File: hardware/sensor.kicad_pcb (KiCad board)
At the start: 2 copper layers, 10 parts, among them U1 ESP32-WROOM, U2 AP2112K-3.3TRG1, U3 BME280

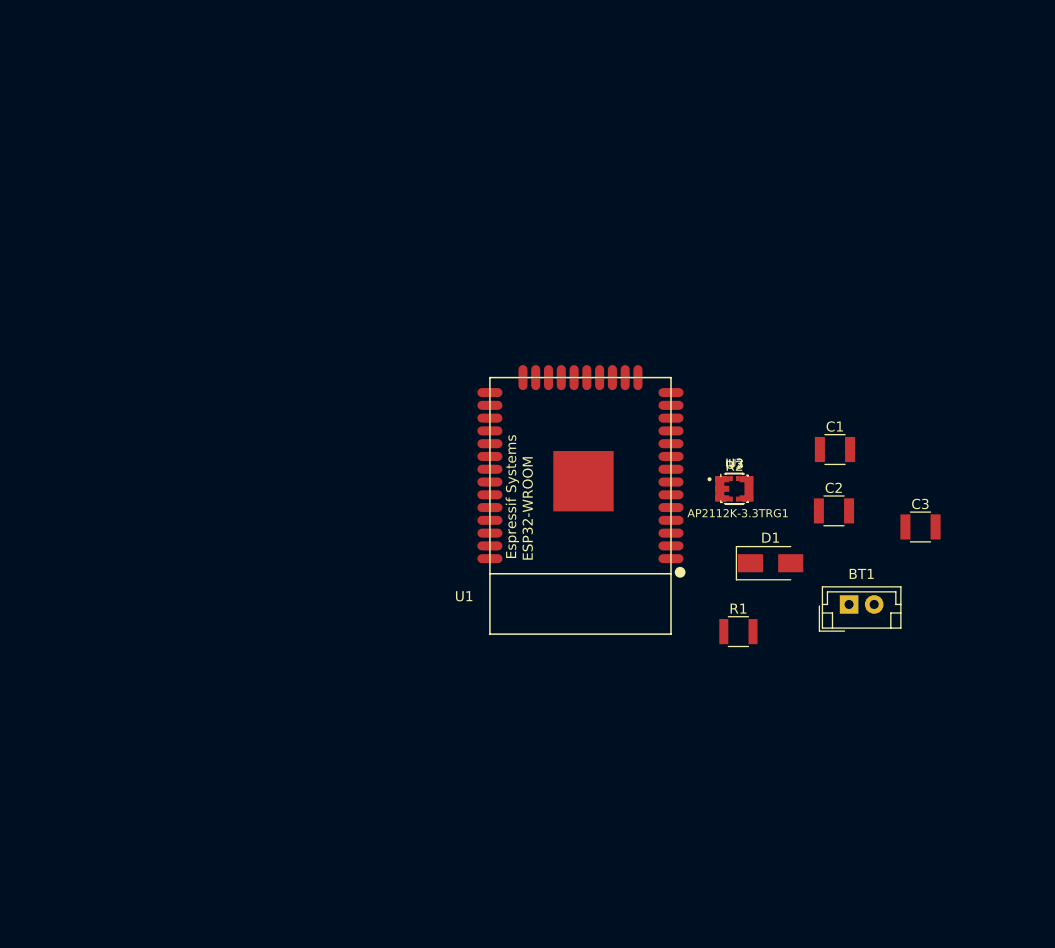
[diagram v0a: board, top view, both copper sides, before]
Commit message: Continue schematic work
Cleanup power
Add I2C connectors
Connect BME280 w/ I2C
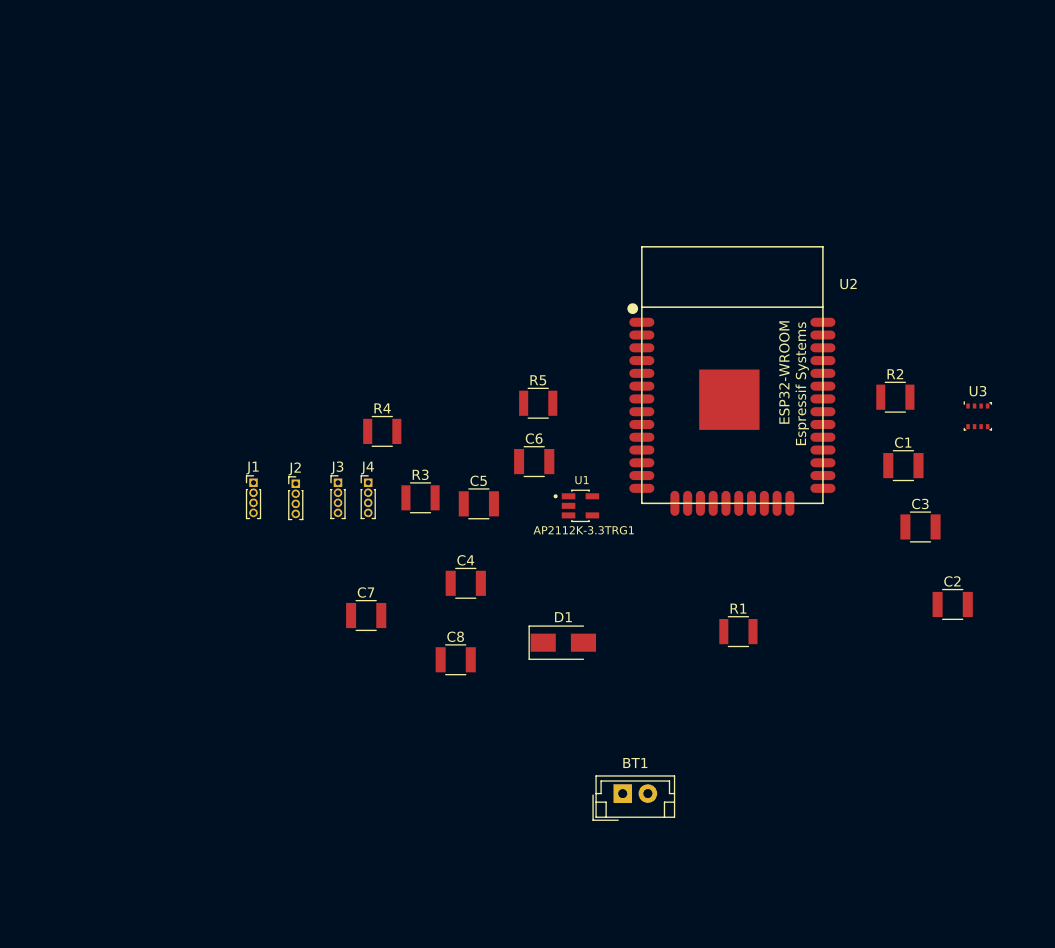
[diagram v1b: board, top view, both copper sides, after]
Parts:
- added C4: 1uF, Capacitors_SMD:C_1210, F.Cu at (121.8, 114.4)
- added C5: 10uF, Capacitors_SMD:C_1210, F.Cu at (123.1, 106.5)
- added C6: 0.1uF, Capacitors_SMD:C_1210, F.Cu at (128.6, 102.3)
- added C7: 100nF, Capacitors_SMD:C_1210, F.Cu at (111.9, 117.6)
- added C8: 100nF, Capacitors_SMD:C_1210, F.Cu at (120.8, 122.0)
- added J1: Conn_01x04, Pin_Headers:Pin_Header_Straight_1x04_Pitch1.00mm, F.Cu at (100.7, 104.4)
- added J2: Conn_01x04, Pin_Headers:Pin_Header_Straight_1x04_Pitch1.00mm, F.Cu at (104.9, 104.5)
- added J3: Conn_01x04, Pin_Headers:Pin_Header_Straight_1x04_Pitch1.00mm, F.Cu at (109.1, 104.4)
- added J4: Conn_01x04, Pin_Headers:Pin_Header_Straight_1x04_Pitch1.00mm, F.Cu at (112.1, 104.4)
- added R3: 10k, Resistors_SMD:R_1210, F.Cu at (117.3, 105.9)
- added R4: 4.7k, Resistors_SMD:R_1210, F.Cu at (113.5, 99.3)
- added R5: 4.7k, Resistors_SMD:R_1210, F.Cu at (129.0, 96.5)
- C2: value 10uF -> 0.1uF
- C3: value 1uF -> 10uF
- U1: value ESP32-WROOM -> AP2112K-3.3TRG1; footprint ESP32-footprints-Lib:ESP32-WROOM -> AP2112K-3.3TRG1:SOT95P285X140-5N
- U2: value AP2112K-3.3TRG1 -> ESP32-WROOM; footprint AP2112K-3.3TRG1:SOT95P285X140-5N -> ESP32-footprints-Lib:ESP32-WROOM
- moved BT1 29.3 mm to (137.4, 135.3)
- moved U3 25.2 mm to (172.7, 97.8)
- moved D1 22.1 mm to (131.5, 120.3)
- moved R2 18.4 mm to (164.5, 95.9)
- moved C2 15.0 mm to (170.2, 116.5)
- moved U2 11.3 mm to (148.3, 93.7), turned to 180 degrees
- moved C1 6.99 mm to (165.3, 102.7)
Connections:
- C2 pad 1: VCC -> Net-(C2-Pad1)
- U1 pad 1: GND -> Net-(C1-Pad1)
- U1 pad 2: VCC -> GND
- U1 pad 3: VCC -> Net-(C1-Pad1)
- U1 pad 5: (no net) -> VCC
- U2 pad 1: Net-(C1-Pad1) -> GND
- U2 pad 2: GND -> VCC
- U2 pad 3: Net-(C1-Pad1) -> Net-(C2-Pad1)
- U2 pad 5: VCC -> (no net)
- U3 pad 2: (no net) -> VCC
- U3 pad 3: (no net) -> iic1_sda
- U3 pad 4: (no net) -> iic1_clk
- U3 pad 5: (no net) -> GND

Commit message: Continue HW design
* Setup SPI expansion connectors
* Re-annotate caps for power regulator and WROOM power
* Add globals for JTAG pins
* Rough grouping of parts on PCB
- Note - still need to make battery setup choices and footprint choices for passives
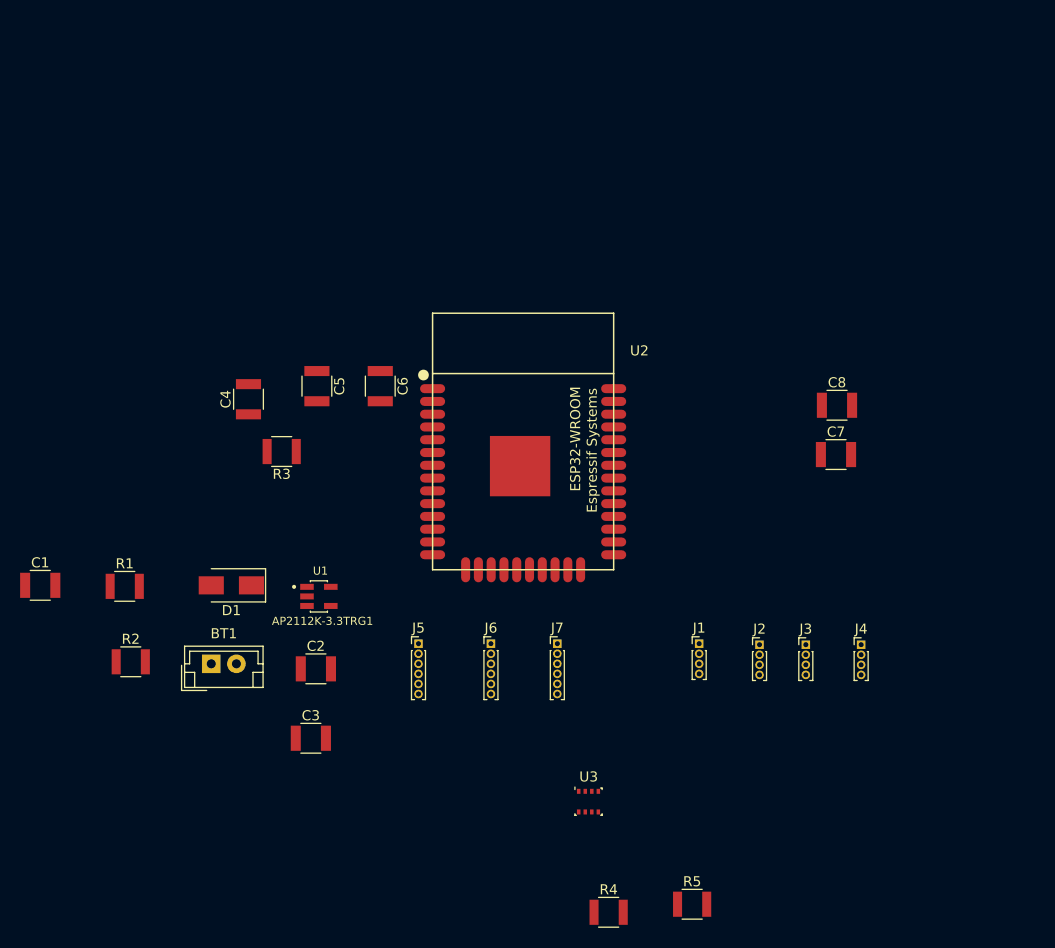
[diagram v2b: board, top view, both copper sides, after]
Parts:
- added J5: Conn_01x06, Pin_Headers:Pin_Header_Straight_1x06_Pitch1.00mm, F.Cu at (117.1, 120.4)
- added J6: Conn_01x06, Pin_Headers:Pin_Header_Straight_1x06_Pitch1.00mm, F.Cu at (124.3, 120.4)
- added J7: Conn_01x06, Pin_Headers:Pin_Header_Straight_1x06_Pitch1.00mm, F.Cu at (130.9, 120.4)
- C2: value 0.1uF -> 10uF
- C3: value 10uF -> 1uF
- C4: value 1uF -> 0.1uF
- moved C1 86.6 mm to (79.5, 114.6)
- moved R2 80.4 mm to (88.5, 122.2)
- moved C3 64.1 mm to (106.4, 129.8)
- moved C2 63.6 mm to (106.9, 122.9)
- moved R1 61.2 mm to (87.9, 114.7)
- moved U3 54.4 mm to (134.0, 136.1)
- moved R4 52.8 mm to (136.0, 147.1)
- moved R5 52.1 mm to (144.3, 146.3)
- moved J4 51.6 mm to (161.1, 120.5)
- moved C7 49.4 mm to (158.6, 101.6)
- moved J3 49.2 mm to (155.6, 120.5)
- moved J2 48.8 mm to (151.0, 120.5)
- moved J1 47.1 mm to (145.0, 120.4)
- moved C8 45.6 mm to (158.7, 96.7)
- moved BT1 42.9 mm to (96.5, 122.4)
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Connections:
- C2 pad 1: Net-(C2-Pad1) -> VCC
- C4 pad 1: VCC -> Net-(C4-Pad1)
- R3 pad 2: Net-(C2-Pad1) -> Net-(C4-Pad1)
- U2 pad 10: (no net) -> spi1_clk
- U2 pad 11: (no net) -> spi1_mosi
- U2 pad 12: (no net) -> spi1_miso
- U2 pad 13: (no net) -> jt_mtms
- U2 pad 14: (no net) -> jt_mtdi
- U2 pad 16: (no net) -> jt_mtck
- U2 pad 17: (no net) -> Net-(U2-Pad17)
- U2 pad 18: (no net) -> Net-(U2-Pad18)
- U2 pad 19: (no net) -> Net-(U2-Pad19)
- U2 pad 20: (no net) -> Net-(U2-Pad20)
- U2 pad 21: (no net) -> Net-(U2-Pad21)
- U2 pad 22: (no net) -> Net-(U2-Pad22)
- U2 pad 23: (no net) -> jt_mtdo
- U2 pad 24: (no net) -> Net-(U2-Pad24)
- U2 pad 25: (no net) -> jt_prog
- U2 pad 26: (no net) -> Net-(U2-Pad26)
- U2 pad 29: (no net) -> Net-(U2-Pad29)
- U2 pad 3: Net-(C2-Pad1) -> Net-(C4-Pad1)
- U2 pad 32: (no net) -> Net-(U2-Pad32)
- U2 pad 33: (no net) -> Net-(U2-Pad33)
- U2 pad 34: (no net) -> Net-(U2-Pad34)
- U2 pad 35: (no net) -> Net-(U2-Pad35)
- U2 pad 36: (no net) -> Net-(U2-Pad36)
- U2 pad 37: (no net) -> Net-(U2-Pad37)
- U2 pad 4: (no net) -> Net-(U2-Pad4)
- U2 pad 5: (no net) -> Net-(U2-Pad5)
- U2 pad 7: (no net) -> spi1_ssa
- U2 pad 8: (no net) -> spi1_ssb
- U2 pad 9: (no net) -> spi1_ssc

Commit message: Additional fixes, Place & route board
* Add junction on C9 to GND
* Swap SPI pins for cleaner routing
* Finish initial routing of board

TODO: Finish silkscreen layout
* Reference labels
* Page labels
* Board version markings
* Art
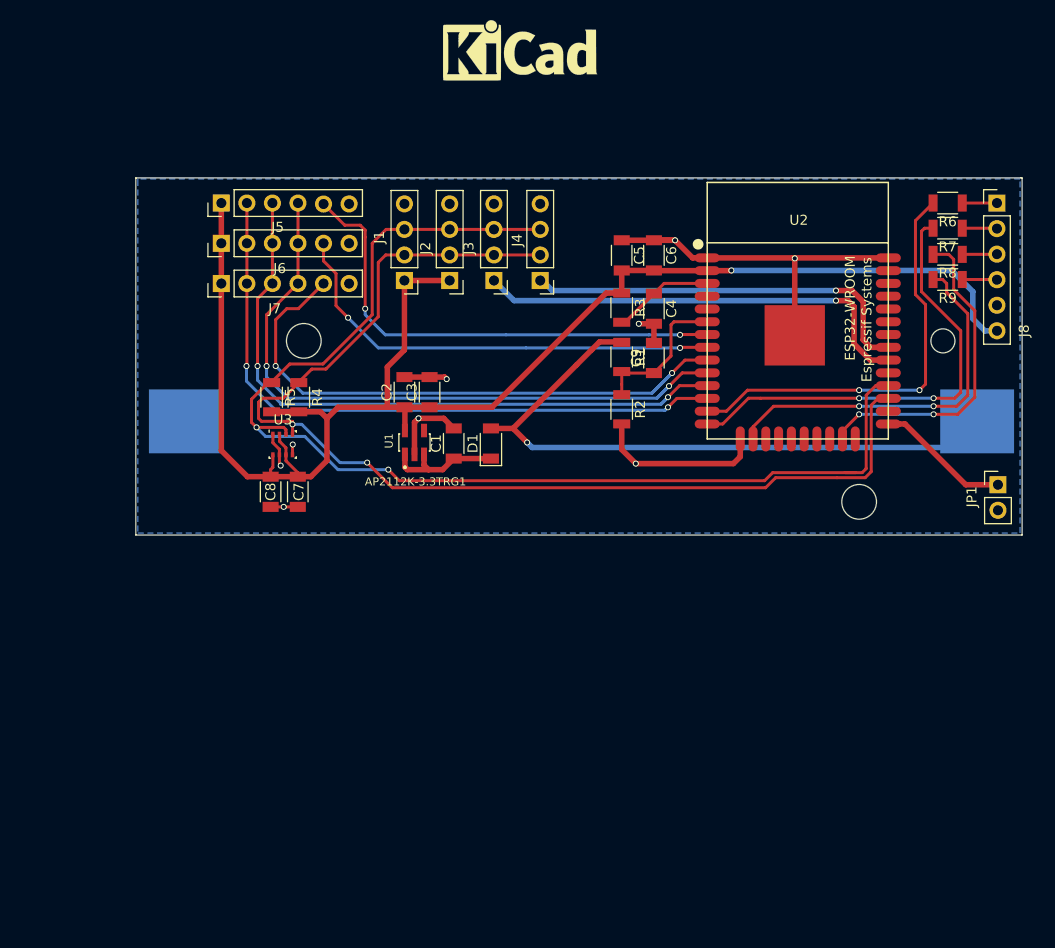
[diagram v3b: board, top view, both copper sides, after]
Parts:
- added C9: 0.1uF, Capacitors_SMD:C_1206, F.Cu at (140.5, 92.0)
- added J8: Conn_01x06, Pin_Headers:Pin_Header_Straight_1x06_Pitch2.54mm, F.Cu at (174.6, 76.6)
- added JP1: Jumper_NO_Small, Pin_Headers:Pin_Header_Straight_1x02_Pitch2.54mm, F.Cu at (174.7, 104.6)
- added R6: 100, Resistors_SMD:R_1206, F.Cu at (169.7, 76.6)
- added R7: 100, Resistors_SMD:R_1206, F.Cu at (169.7, 79.1)
- added R8: 100, Resistors_SMD:R_1206, F.Cu at (169.7, 81.7)
- added R9: 100, Resistors_SMD:R_1206, F.Cu at (169.7, 84.2)
- added REF***: KiCad-Logo_6mm_SilkScreen, Symbols:KiCad-Logo_6mm_SilkScreen, F.Cu at (127.2, 61.4)
- BT1: footprint Connectors_JST:JST_EH_B02B-EH-A_02x2.50mm_Straight -> Battery_Holders:Keystone_1042_1x18650; moved to B.Cu
- C1, C2, C3, C4, C5, C6, C7, C8: footprint Capacitors_SMD:C_1210 -> Capacitors_SMD:C_1206
- D1: footprint Diodes_SMD:D_SMA -> Diodes_SMD:D_1206
- J1, J2, J3, J4: footprint Pin_Headers:Pin_Header_Straight_1x04_Pitch1.00mm -> Pin_Headers:Pin_Header_Straight_1x04_Pitch2.54mm
- J5, J6, J7: footprint Pin_Headers:Pin_Header_Straight_1x06_Pitch1.00mm -> Pin_Headers:Pin_Header_Straight_1x06_Pitch2.54mm
- R1: value R -> 10k; footprint Resistors_SMD:R_1210 -> Resistors_SMD:R_1206
- R2: value R -> 3.3k; footprint Resistors_SMD:R_1210 -> Resistors_SMD:R_1206
- R3, R4, R5: footprint Resistors_SMD:R_1210 -> Resistors_SMD:R_1206
- moved R5 65.5 mm to (102.5, 95.9), turned to 270 degrees
- moved R4 59.8 mm to (105.2, 95.9), turned to 270 degrees
- moved C7 56.3 mm to (102.4, 105.3), turned to 90 degrees
- moved R2 54.9 mm to (137.3, 97.1), turned to 270 degrees
- moved R1 54.4 mm to (137.3, 91.9), turned to 270 degrees
- moved C8 54.3 mm to (105.1, 105.3), turned to 90 degrees
- moved J7 49.0 mm to (97.5, 84.6), turned to 90 degrees
- moved J4 48.2 mm to (129.2, 84.3), turned to 180 degrees
- moved J5 48.0 mm to (97.5, 76.6), turned to 90 degrees
- moved J6 48.0 mm to (97.5, 80.6), turned to 90 degrees
- moved J3 47.7 mm to (124.6, 84.3), turned to 180 degrees
- moved J2 47.5 mm to (120.2, 84.3), turned to 180 degrees
- moved U3 46.7 mm to (103.6, 100.6)
- moved J1 46.5 mm to (115.7, 84.3), turned to 180 degrees
- moved BT1 44.0 mm to (133.3, 98.3), turned to 180 degrees
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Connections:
- U2 pad 10: spi1_clk -> spi1_miso
- U2 pad 12: spi1_miso -> spi1_clk
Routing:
- net VCC: track 0.00 -> 154.9 mm, vias 0 -> 1
- net iic1_sda: track 0.00 -> 121.7 mm, vias 0 -> 2
- net iic1_clk: track 0.00 -> 113.5 mm, vias 0 -> 2
- net GND: track 0.00 -> 77.2 mm, vias 0 -> 9
- net Net-(BT1-Pad1): track 0.00 -> 67.8 mm, vias 0 -> 1
- net spi1_miso: track 0.00 -> 66.0 mm, vias 0 -> 2
- net spi1_mosi: track 0.00 -> 65.7 mm, vias 0 -> 2
- net spi1_clk: track 0.00 -> 65.6 mm, vias 0 -> 2
- net spi1_ssc: track 0.00 -> 59.1 mm, vias 0 -> 2
- net spi1_ssa: track 0.00 -> 48.5 mm, vias 0 -> 2
- net jt_mtdi: track 0.00 -> 45.4 mm, vias 0 -> 2
- net spi1_ssb: track 0.00 -> 45.4 mm, vias 0 -> 2
- net iic1_en1: track 0.00 -> 44.6 mm, vias 0 -> 1
- net jt_mtms: track 0.00 -> 42.0 mm, vias 0 -> 2
- net iic1_en2: track 0.00 -> 39.6 mm, vias 0 -> 1
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- added copper zone on B.Cu, net GND
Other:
- board outline added: 88.1 x 35.5 mm
- net class Default: trace_width 0.25 -> 0.3
- net class data added: clearance 0.2, trace_width 0.3, via_dia 0.6, via_drill 0.4
- net class power added: clearance 0.25, trace_width 0.55, via_dia 0.6, via_drill 0.4
- net class tiny added: clearance 0.153, trace_width 0.153, via_dia 0.4, via_drill 0.3
- rule trace_min: 0.2 -> 0.153

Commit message: V1.0 board done
* Refs updated
* version info added

Note - For now, we're leaving the gerber output directory out of the github project
Sensor.csv is early BOM

TODO:
* Update hardware markdown with new pin info, including board references
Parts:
- removed the REF*** at (127.2, 61.4)
- added REF***: KiCad-Logo2_12mm_SilkScreen, Symbols:KiCad-Logo2_12mm_SilkScreen, B.Cu at (159.7, 81.3)
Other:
- board text added: "Board version 1.0"
- board text added: "RaspiCool Environment Sensor"
